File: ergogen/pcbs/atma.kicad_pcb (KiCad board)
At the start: 2 copper layers, 99.8 x 100 mm, 24 parts

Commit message: atma v0.2.0 (#2)
* atma v0.2.0
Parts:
- removed _6: , MountingHole_2.2mm_M2_Pad_Via
- moved ? 97.7 mm to (154.3, 172.4)
- moved _5 46.9 mm to (237.9, 166.7)
- moved _4 42.6 mm to (199.9, 123.8)
- moved ? 24.7 mm to (246.5, 121.7)
- moved _3 19.1 mm to (161.9, 142.9)
- moved S16 14.4 mm to (209.4, 176.2)
- moved S17 14.4 mm to (228.4, 176.2)
- moved S18 14.4 mm to (247.4, 176.2)
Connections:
- ? pad 1: matrix_pinky_bottom -> matrix_pinky_top
- ? pad 10: GP9 -> matrix_index_bottom
- ? pad 11: matrix_middle_top -> matrix_index_home
- ? pad 12: matrix_inner_bottom -> matrix_index_top
- ? pad 13: matrix_inner_home -> GP12
- ? pad 14: matrix_inner_top -> GP13
- ? pad 15: matrix_index_top -> matrix_inner_top
- ? pad 16: matrix_index_home -> matrix_inner_home
- ? pad 17: matrix_index_bottom -> matrix_inner_bottom
- ? pad 18: thumbfan_far_home -> thumbfan_near_home
- ? pad 20: thumbfan_near_home -> thumbfan_far_home
- ? pad 3: matrix_pinky_top -> matrix_pinky_bottom
- ? pad 4: matrix_ring_top -> matrix_ring_bottom
- ? pad 6: matrix_ring_bottom -> matrix_ring_top
- ? pad 7: matrix_middle_bottom -> matrix_middle_top
- ? pad 9: GP8 -> matrix_middle_bottom
- ? pad 3: GP8 -> GP13
- ? pad 4: GP8 -> GP13
- ? pad 5: GP9 -> GP12
- ? pad 6: GP9 -> GP12
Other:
- board size 99.8 x 100 mm -> 114.1 x 81 mm
- board text added: "JLCJLCJLCJLC"
- board text added: "atma v0.2.0"

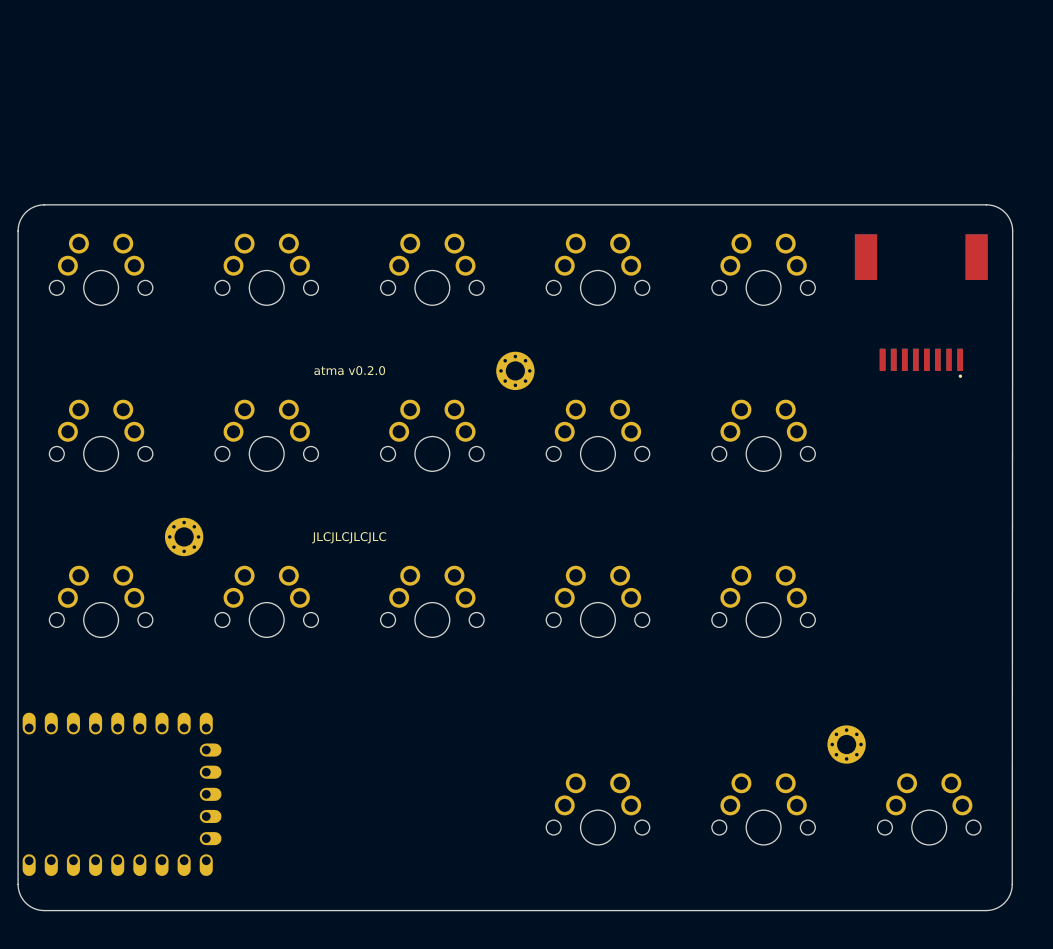
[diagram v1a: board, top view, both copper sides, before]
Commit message: Pi Pico, Kong-style thumbs, hotswap, encoder
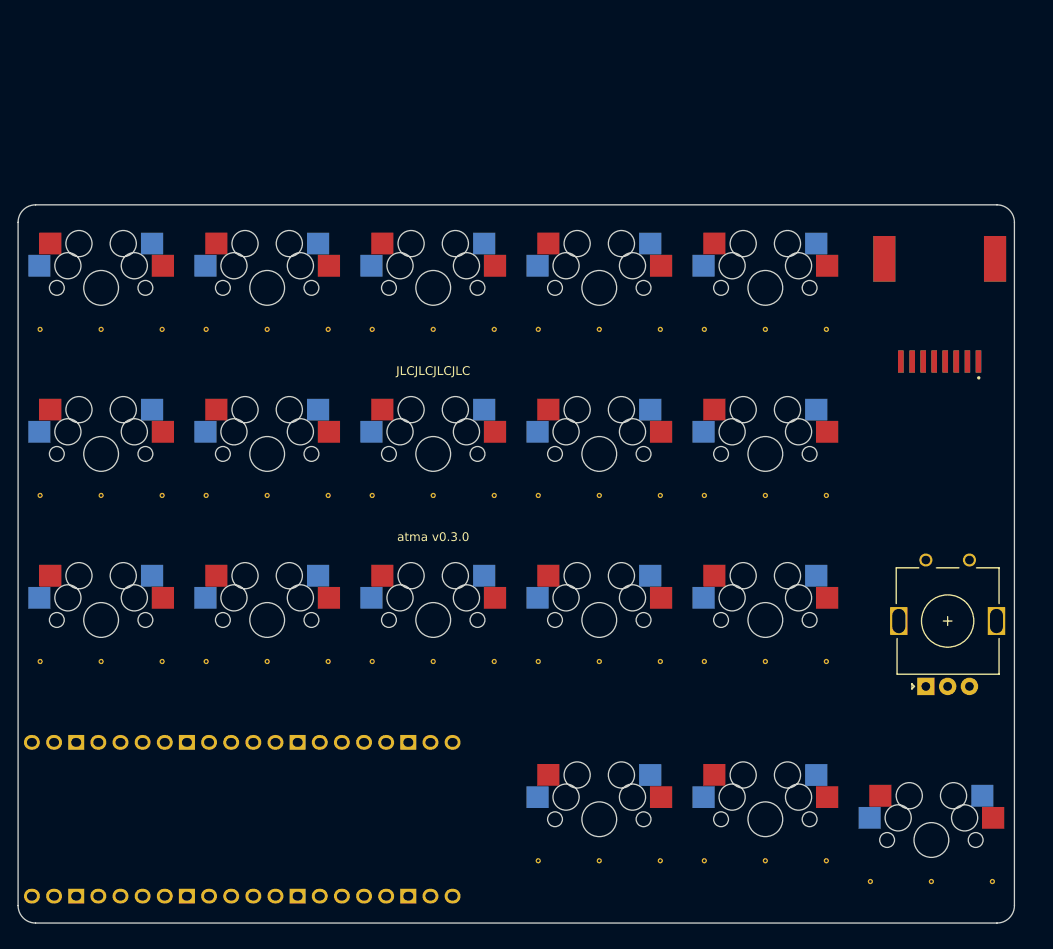
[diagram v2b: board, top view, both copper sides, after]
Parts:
- removed the ? at (154.3, 172.4)
- removed _3, _4, _5: , MountingHole_2.2mm_M2_Pad_Via
- added REF**: VIA-0.6mm, VIA-0.6mm, F.Cu at (152.4, 157.2)
- added REF**: VIA-0.6mm, VIA-0.6mm, F.Cu at (209.6, 157.2)
- added REF**: VIA-0.6mm, VIA-0.6mm, F.Cu at (209.6, 138.1)
- added REF**: VIA-0.6mm, VIA-0.6mm, F.Cu at (209.6, 119.1)
- added REF**: VIA-0.6mm, VIA-0.6mm, F.Cu at (228.6, 157.2)
- added REF**: VIA-0.6mm, VIA-0.6mm, F.Cu at (228.6, 138.1)
- added REF**: VIA-0.6mm, VIA-0.6mm, F.Cu at (228.6, 119.1)
- added REF**: VIA-0.6mm, VIA-0.6mm, F.Cu at (209.6, 180.0)
- added REF**: VIA-0.6mm, VIA-0.6mm, F.Cu at (228.6, 180.0)
- added REF**: VIA-0.6mm, VIA-0.6mm, F.Cu at (247.7, 182.4)
- added REF**: VIA-0.6mm, VIA-0.6mm, F.Cu at (145.4, 157.2)
- added REF**: VIA-0.6mm, VIA-0.6mm, F.Cu at (152.4, 138.1)
- added REF**: VIA-0.6mm, VIA-0.6mm, F.Cu at (145.4, 138.1)
- added REF**: VIA-0.6mm, VIA-0.6mm, F.Cu at (145.4, 119.1)
- added REF**: VIA-0.6mm, VIA-0.6mm, F.Cu at (164.5, 157.2)
- added REF**: VIA-0.6mm, VIA-0.6mm, F.Cu at (164.5, 138.1)
- added REF**: VIA-0.6mm, VIA-0.6mm, F.Cu at (164.5, 119.1)
- added REF**: VIA-0.6mm, VIA-0.6mm, F.Cu at (183.5, 157.2)
- added REF**: VIA-0.6mm, VIA-0.6mm, F.Cu at (183.5, 138.1)
- added REF**: VIA-0.6mm, VIA-0.6mm, F.Cu at (183.5, 119.1)
- added REF**: VIA-0.6mm, VIA-0.6mm, F.Cu at (202.6, 157.2)
- added REF**: VIA-0.6mm, VIA-0.6mm, F.Cu at (202.6, 138.1)
- added REF**: VIA-0.6mm, VIA-0.6mm, F.Cu at (152.4, 119.1)
- added REF**: VIA-0.6mm, VIA-0.6mm, F.Cu at (202.6, 119.1)
- added REF**: VIA-0.6mm, VIA-0.6mm, F.Cu at (221.6, 157.2)
- added REF**: VIA-0.6mm, VIA-0.6mm, F.Cu at (221.6, 138.1)
- added REF**: VIA-0.6mm, VIA-0.6mm, F.Cu at (221.6, 119.1)
- added REF**: VIA-0.6mm, VIA-0.6mm, F.Cu at (202.6, 180.0)
- added REF**: VIA-0.6mm, VIA-0.6mm, F.Cu at (221.6, 180.0)
- added REF**: VIA-0.6mm, VIA-0.6mm, F.Cu at (240.7, 182.4)
- added REF**: VIA-0.6mm, VIA-0.6mm, F.Cu at (159.4, 157.2)
- added REF**: VIA-0.6mm, VIA-0.6mm, F.Cu at (159.4, 138.1)
- added REF**: VIA-0.6mm, VIA-0.6mm, F.Cu at (159.4, 119.1)
- added REF**: VIA-0.6mm, VIA-0.6mm, F.Cu at (171.5, 157.2)
- added REF**: VIA-0.6mm, VIA-0.6mm, F.Cu at (178.5, 157.2)
- added REF**: VIA-0.6mm, VIA-0.6mm, F.Cu at (178.5, 138.1)
- added REF**: VIA-0.6mm, VIA-0.6mm, F.Cu at (178.5, 119.1)
- added REF**: VIA-0.6mm, VIA-0.6mm, F.Cu at (197.5, 157.2)
- added REF**: VIA-0.6mm, VIA-0.6mm, F.Cu at (197.5, 138.1)
- added REF**: VIA-0.6mm, VIA-0.6mm, F.Cu at (197.5, 119.1)
- added REF**: VIA-0.6mm, VIA-0.6mm, F.Cu at (216.6, 157.2)
- added REF**: VIA-0.6mm, VIA-0.6mm, F.Cu at (216.6, 138.1)
- added REF**: VIA-0.6mm, VIA-0.6mm, F.Cu at (216.6, 119.1)
- added REF**: VIA-0.6mm, VIA-0.6mm, F.Cu at (235.6, 157.2)
- added REF**: VIA-0.6mm, VIA-0.6mm, F.Cu at (171.5, 138.1)
- added REF**: VIA-0.6mm, VIA-0.6mm, F.Cu at (235.6, 138.1)
- added REF**: VIA-0.6mm, VIA-0.6mm, F.Cu at (235.6, 119.1)
- added REF**: VIA-0.6mm, VIA-0.6mm, F.Cu at (216.6, 180.0)
- added REF**: VIA-0.6mm, VIA-0.6mm, F.Cu at (235.6, 180.0)
- added REF**: VIA-0.6mm, VIA-0.6mm, F.Cu at (254.7, 182.4)
- added REF**: VIA-0.6mm, VIA-0.6mm, F.Cu at (171.5, 119.1)
- added REF**: VIA-0.6mm, VIA-0.6mm, F.Cu at (190.5, 157.2)
- added REF**: VIA-0.6mm, VIA-0.6mm, F.Cu at (190.5, 138.1)
- added REF**: VIA-0.6mm, VIA-0.6mm, F.Cu at (190.5, 119.1)
- added U0: , RPi_Pico_TH_oval_face_down, F.Cu at (168.6, 175.3)
- added _2: , rotary_encoder, F.Cu at (249.6, 152.4)
- moved ? 2.11 mm to (248.6, 121.9)
- moved S18 1.45 mm to (247.7, 177.6)
- moved S17 0.97 mm to (228.6, 175.3)
- moved S16 0.96 mm to (209.6, 175.3)
- moved S13 0.20 mm to (228.6, 152.4)
- moved S14 0.20 mm to (228.6, 133.3)
- moved S15 0.20 mm to (228.6, 114.3)
- moved S10 0.15 mm to (209.6, 152.4)
- moved S11 0.15 mm to (209.6, 133.3)
- moved S12 0.15 mm to (209.6, 114.3)
- moved S7 0.10 mm to (190.5, 152.4)
- moved S8 0.10 mm to (190.5, 133.3)
- moved S9 0.10 mm to (190.5, 114.3)
- moved S4 0.05 mm to (171.5, 152.4)
- moved S5 0.05 mm to (171.5, 133.3)
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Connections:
- net 3V3 renamed VSYS
- net GP12 renamed GP16
- net GP13 renamed GP17
- S16 pad 1: thumbfan_near_home -> thumb_near_home
- S17 pad 1: thumbfan_home_home -> thumb_middle_home
- S18 pad 1: thumbfan_far_home -> thumb_far_home
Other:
- board size 114.1 x 81 mm -> 114.3 x 82.4 mm
- board text added: "atma v0.3.0"
- board text removed: "atma v0.2.0"

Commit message: rp2040 zero
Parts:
- removed the REF** at (152.4, 157.2)
- removed the REF** at (209.6, 157.2)
- removed the REF** at (209.6, 138.1)
- removed the REF** at (209.6, 119.1)
- removed the REF** at (228.6, 157.2)
- removed the REF** at (228.6, 138.1)
- removed the REF** at (228.6, 119.1)
- removed the REF** at (209.6, 180.0)
- removed the REF** at (228.6, 180.0)
- removed the REF** at (247.7, 182.4)
- removed the REF** at (152.4, 138.1)
- removed the REF** at (152.4, 119.1)
- removed the REF** at (171.5, 157.2)
- removed the REF** at (171.5, 138.1)
- removed the REF** at (171.5, 119.1)
- removed the REF** at (190.5, 157.2)
- removed the REF** at (190.5, 138.1)
- removed the REF** at (190.5, 119.1)
- removed U0: , RPi_Pico_TH_oval_face_down
- removed _2: , rotary_encoder
- added ?: , rp2040_zero_tht_pads, F.Cu at (154.4, 173.4)
- moved ? 0.97 mm to (247.7, 121.7)
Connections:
- net GP16 renamed GP12
- net GP17 renamed GP13
- net thumb_far_home renamed thumb_far_mods
- net thumb_middle_home renamed thumb_middle_mods
- net thumb_near_home renamed thumb_near_mods
- ? pad 1: VSYS -> 3V3
- ? pad 8: VSYS -> 3V3
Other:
- outline, holes or cut-outs redrawn
- board text added: "atma v1.0.0"
- board text removed: "atma v0.3.0"

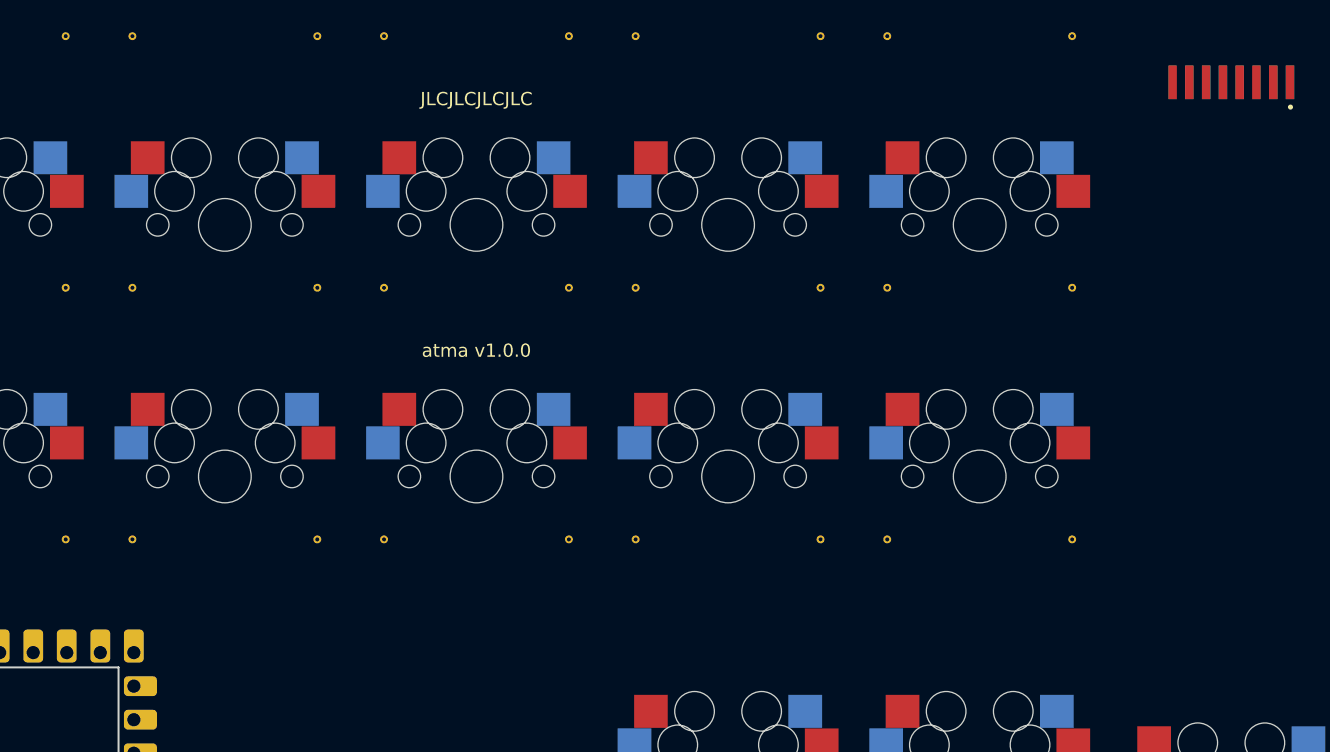
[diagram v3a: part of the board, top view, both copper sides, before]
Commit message: adding outlines for case
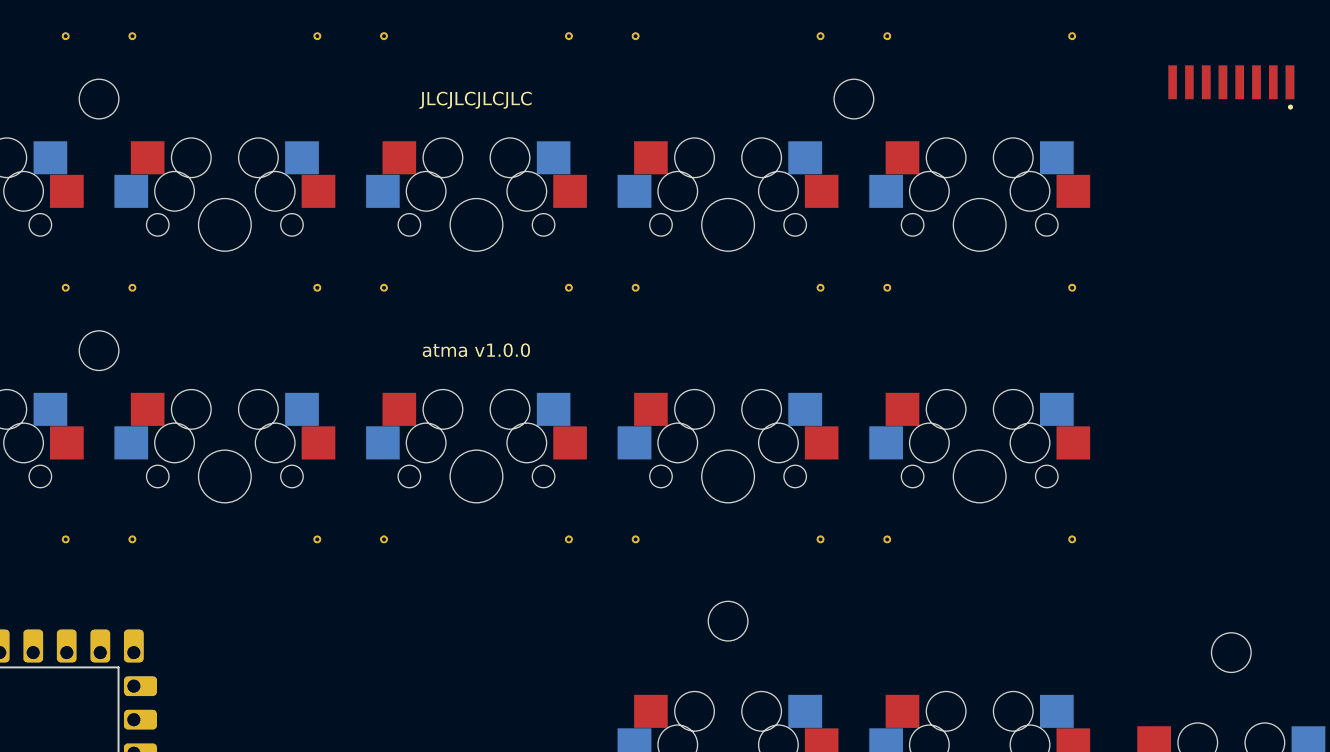
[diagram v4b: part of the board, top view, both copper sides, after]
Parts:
- added ?: , DrillHole, F.Cu at (209.6, 163.4)
- added ?: , DrillHole, F.Cu at (247.7, 165.7)
- added ?: , DrillHole, F.Cu at (161.9, 123.8)
- added ?: , DrillHole, F.Cu at (161.9, 142.9)
- added ?: , DrillHole, F.Cu at (219.1, 123.8)
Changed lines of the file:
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@@
                 (effects (font (size 1 1) (thickness 0.15)) )
             )
+      (module DrillHole (layer "F.Cu")
+      (at 209.55 163.35375 0)
+      (pad "" np_thru_hole circle (at 0 0) (size 3 3) (drill 3) (layers *.Cu *.Mask))
+    )
+      (module DrillHole (layer "F.Cu")
+      (at 247.65 165.73499999999999 0)
+      (pad "" np_thru_hole circle (at 0 0) (size 3 3) (drill 3) (layers *.Cu *.Mask))
+    )
+      (module DrillHole (layer "F.Cu")
+      (at 161.925 123.82499999999999 0)
+      (pad "" np_thru_hole circle (at 0 0) (size 3 3) (drill 3) (layers *.Cu *.Mask))
+    )
+      (module DrillHole (layer "F.Cu")
+      (at 161.925 142.875 0)
+      (pad "" np_thru_hole circle (at 0 0) (size 3 3) (drill 3) (layers *.Cu *.Mask))
+    )
+      (module DrillHole (layer "F.Cu")
+      (at 219.07500000000002 123.82499999999999 0)
+      (pad "" np_thru_hole circle (at 0 0) (size 3 3) (drill 3) (layers *.Cu *.Mask))
+    )
             (gr_line (start 142.875 186.16625) (end 142.875 179.85500000000002) (angle 90) (layer Edge.Cuts) (width 0.15))
 (gr_line (start 142.875 166.85500000000002) (end 142.875 105.77499999999999) (angle 90) (layer Edge.Cuts) (width 0.15))
